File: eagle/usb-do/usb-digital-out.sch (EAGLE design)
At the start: 9 parts, among them IC2 PIC32MX795F512L, IC3 USB-UART-FT234XD, X2 MINI-USB-32005-201

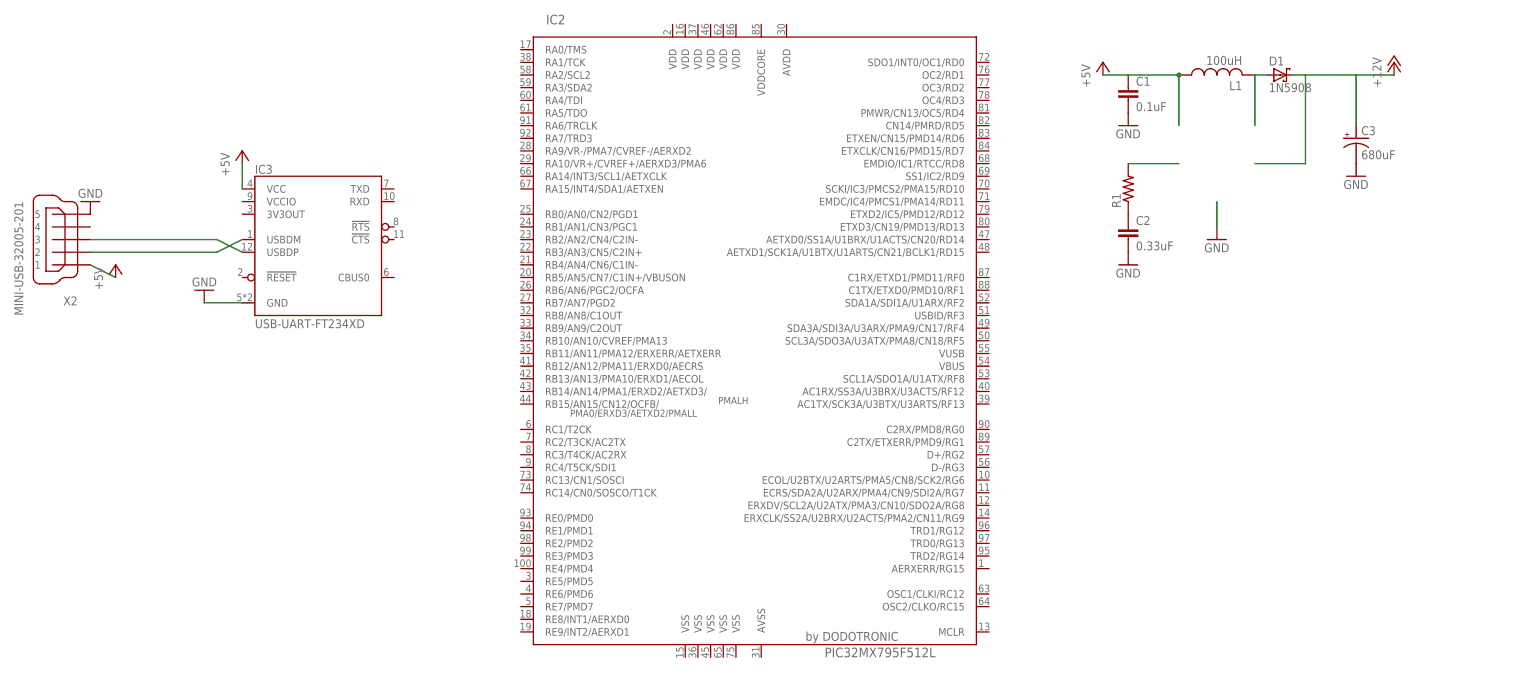
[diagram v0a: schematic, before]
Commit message: updated USB schematic with LM2577-12
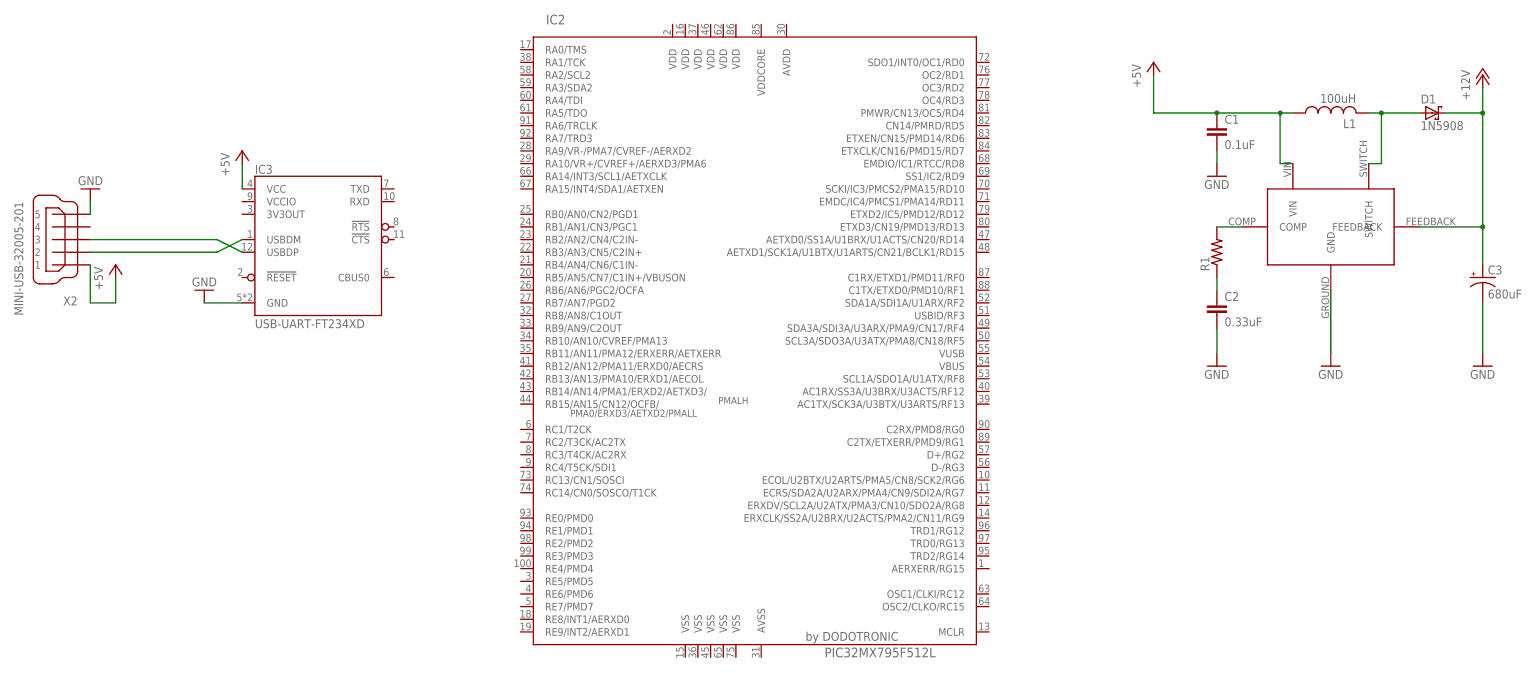
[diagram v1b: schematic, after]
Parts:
- added U$1: LM2577, nusolar_components:LM2577
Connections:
- net +12V: now also U$1.FEEDBACK
- net +5V: now also U$1.VIN
- net GND: now also U$1.GND
- net N$2: now also R1.2, U$1.COMP; no longer D1.A, L1.2
- net N$3: now also D1.A, L1.2, U$1.SWITCH; no longer R1.2
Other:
- moved on the sheet: C1, C2, C3, D1, L1, R1
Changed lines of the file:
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@@
 <part name="IC2" library="DodoMicroR3" deviceset="PIC32MX795F512" device="L"/>
 <part name="IC3" library="11-egna-ic" deviceset="USB-UART-FT234XD" device=""/>
+<part name="U$1" library="nusolar_components" deviceset="LM2577" device=""/>
 </parts>
 <sheets>
@@
 </plain>
 <instances>
-<instance part="P+1" gate="1" x="152.4" y="81.28"/>
-<instance part="C1" gate="G$1" x="157.48" y="76.2"/>
-<instance part="C2" gate="G$1" x="157.48" y="48.26"/>
-<instance part="GND1" gate="1" x="157.48" y="68.58"/>
-<instance part="GND2" gate="1" x="157.48" y="40.64"/>
-<instance part="GND3" gate="1" x="175.26" y="45.72"/>
-<instance part="GND4" gate="1" x="203.2" y="58.42"/>
-<instance part="R1" gate="G$1" x="157.48" y="55.88" rot="R90"/>
-<instance part="C3" gate="G$1" x="203.2" y="66.04"/>
-<instance part="L1" gate="G$1" x="175.26" y="78.74" rot="R90"/>
-<instance part="D1" gate="1" x="187.96" y="78.74"/>
-<instance part="P+2" gate="1" x="210.82" y="81.28"/>
+<instance part="P+1" gate="1" x="162.56" y="81.28"/>
+<instance part="C1" gate="G$1" x="175.26" y="68.58"/>
+<instance part="C2" gate="G$1" x="175.26" y="33.02"/>
+<instance part="GND1" gate="1" x="175.26" y="58.42"/>
+<instance part="GND2" gate="1" x="175.26" y="20.32"/>
+<instance part="GND3" gate="1" x="198.12" y="20.32"/>
+<instance part="GND4" gate="1" x="228.6" y="20.32"/>
+<instance part="R1" gate="G$1" x="175.26" y="43.18" rot="R90"/>
+<instance part="C3" gate="G$1" x="228.6" y="38.1"/>
+<instance part="L1" gate="G$1" x="198.12" y="71.12" rot="R90"/>
+<instance part="D1" gate="1" x="218.44" y="71.12"/>
+<instance part="P+2" gate="1" x="228.6" y="78.74"/>
 <instance part="X2" gate="G$1" x="-55.88" y="45.72" rot="R180"/>
 <instance part="P+3" gate="1" x="-45.72" y="40.64"/>
-<instance part="GND5" gate="1" x="-50.8" y="53.34" rot="R180"/>
+<instance part="GND5" gate="1" x="-50.8" y="55.88" rot="R180"/>
 <instance part="GND6" gate="1" x="-27.94" y="35.56" rot="R180"/>
 <instance part="P+4" gate="1" x="-20.32" y="63.5"/>
 <instance part="IC2" gate="G$1" x="86.36" y="22.86"/>
 <instance part="IC3" gate="G$1" x="-5.08" y="43.18"/>
+<instance part="U$1" gate="G$1" x="198.12" y="48.26"/>
 </instances>
 <busses>
@@
 <pinref part="GND1" gate="1" pin="GND"/>
 <pinref part="C1" gate="G$1" pin="2"/>
+<wire x1="175.26" y1="60.96" x2="175.26" y2="63.5" width="0.1524" layer="91"/>
 </segment>
 <segment>
 <pinref part="C2" gate="G$1" pin="2"/>
 <pinref part="GND2" gate="1" pin="GND"/>
+<wire x1="175.26" y1="22.86" x2="175.26" y2="27.94" width="0.1524" layer="91"/>
 </segment>
 <segment>
 <pinref part="GND4" gate="1" pin="GND"/>
 <pinref part="C3" gate="G$1" pin="-"/>
+<wire x1="228.6" y1="22.86" x2="228.6" y2="33.02" width="0.1524" layer="91"/>
 </segment>
 <segment>
 <pinref part="GND3" gate="1" pin="GND"/>
-<wire x1="175.26" y1="48.26" x2="175.26" y2="53.34" width="0.1524" layer="91"/>
+<wire x1="198.12" y1="22.86" x2="198.12" y2="35.56" width="0.1524" layer="91"/>
+<pinref part="U$1" gate="G$1" pin="GND"/>
 </segment>
 <segment>
 <pinref part="X2" gate="G$1" pin="5"/>
 <pinref part="GND5" gate="1" pin="GND"/>
+<wire x1="-50.8" y1="53.34" x2="-50.8" y2="50.8" width="0.1524" layer="91"/>
 </segment>
 <segment>
@@
 <net name="+5V" class="0">
 <segment>
+<pinref part="IC3" gate="G$1" pin="VCC"/>
+<pinref part="P+4" gate="1" pin="+5V"/>
+<wire x1="-20.32" y1="55.88" x2="-20.32" y2="60.96" width="0.1524" layer="91"/>
+</segment>
+<segment>
 <pinref part="P+1" gate="1" pin="+5V"/>
-<wire x1="152.4" y1="78.74" x2="157.48" y2="78.74" width="0.1524" layer="91"/>
+<wire x1="162.56" y1="78.74" x2="162.56" y2="71.12" width="0.1524" layer="91"/>
 <pinref part="C1" gate="G$1" pin="1"/>
+<wire x1="162.56" y1="71.12" x2="175.26" y2="71.12" width="0.1524" layer="91"/>
 <pinref part="L1" gate="G$1" pin="1"/>
-<junction x="167.64" y="78.74"/>
-<wire x1="167.64" y1="78.74" x2="157.48" y2="78.74" width="0.1524" layer="91"/>
-<wire x1="167.64" y1="78.74" x2="167.64" y2="68.58" width="0.1524" layer="91"/>
+<wire x1="175.26" y1="71.12" x2="187.96" y2="71.12" width="0.1524" layer="91"/>
+<junction x="175.26" y="71.12"/>
+<wire x1="187.96" y1="71.12" x2="190.5" y2="71.12" width="0.1524" layer="91"/>
+<wire x1="187.96" y1="71.12" x2="187.96" y2="60.96" width="0.1524" layer="91"/>
+<junction x="187.96" y="71.12"/>
+<pinref part="U$1" gate="G$1" pin="VIN"/>
+<wire x1="187.96" y1="60.96" x2="190.5" y2="60.96" width="0.1524" layer="91"/>
 </segment>
 <segment>
 <pinref part="X2" gate="G$1" pin="1"/>
+<wire x1="-50.8" y1="40.64" x2="-50.8" y2="33.02" width="0.1524" layer="91"/>
+<wire x1="-50.8" y1="33.02" x2="-45.72" y2="33.02" width="0.1524" layer="91"/>
 <pinref part="P+3" gate="1" pin="+5V"/>
-<wire x1="-50.8" y1="40.64" x2="-45.72" y2="38.1" width="0.1524" layer="91"/>
-</segment>
-<segment>
-<pinref part="IC3" gate="G$1" pin="VCC"/>
-<pinref part="P+4" gate="1" pin="+5V"/>
-<wire x1="-20.32" y1="55.88" x2="-20.32" y2="60.96" width="0.1524" layer="91"/>
+<wire x1="-45.72" y1="33.02" x2="-45.72" y2="38.1" width="0.1524" layer="91"/>
 </segment>
 </net>
@@
 <pinref part="C2" gate="G$1" pin="1"/>
 <pinref part="R1" gate="G$1" pin="1"/>
-</segment>
-</net>
-<net name="N$2" class="0">
-<segment>
-<pinref part="L1" gate="G$1" pin="2"/>
-<pinref part="D1" gate="1" pin="A"/>
-<wire x1="182.88" y1="78.74" x2="185.42" y2="78.74" width="0.1524" layer="91"/>
-<wire x1="182.88" y1="78.74" x2="182.88" y2="68.58" width="0.1524" layer="91"/>
-</segment>
-</net>
-<net name="+12V" class="0">
-<segment>
-<pinref part="P+2" gate="1" pin="+12V"/>
-<pinref part="D1" gate="1" pin="C"/>
-<wire x1="210.82" y1="78.74" x2="203.2" y2="78.74" width="0.1524" layer="91"/>
-<pinref part="C3" gate="G$1" pin="+"/>
-<wire x1="203.2" y1="78.74" x2="193.04" y2="78.74" width="0.1524" layer="91"/>
-<wire x1="193.04" y1="78.74" x2="190.5" y2="78.74" width="0.1524" layer="91"/>
-<wire x1="203.2" y1="68.58" x2="203.2" y2="78.74" width="0.1524" layer="91"/>
-<wire x1="193.04" y1="78.74" x2="193.04" y2="60.96" width="0.1524" layer="91"/>
-<wire x1="193.04" y1="60.96" x2="182.88" y2="60.96" width="0.1524" layer="91"/>
-</segment>
-</net>
-<net name="N$3" class="0">
-<segment>
-<pinref part="R1" gate="G$1" pin="2"/>
-<wire x1="157.48" y1="60.96" x2="167.64" y2="60.96" width="0.1524" layer="91"/>
+<wire x1="175.26" y1="35.56" x2="175.26" y2="38.1" width="0.1524" layer="91"/>
 </segment>
 </net>
@@
 </segment>
 </net>
+<net name="N$2" class="0">
+<segment>
+<pinref part="R1" gate="G$1" pin="2"/>
+<pinref part="U$1" gate="G$1" pin="COMP"/>
+<wire x1="175.26" y1="48.26" x2="180.34" y2="48.26" width="0.1524" layer="91"/>
+</segment>
+</net>
+<net name="N$3" class="0">
+<segment>
+<pinref part="L1" gate="G$1" pin="2"/>
+<pinref part="D1" gate="1" pin="A"/>
+<wire x1="205.74" y1="71.12" x2="208.28" y2="71.12" width="0.1524" layer="91"/>
+<pinref part="U$1" gate="G$1" pin="SWITCH"/>
+<wire x1="208.28" y1="71.12" x2="215.9" y2="71.12" width="0.1524" layer="91"/>
+<wire x1="205.74" y1="60.96" x2="208.28" y2="60.96" width="0.1524" layer="91"/>
+<wire x1="208.28" y1="60.96" x2="208.28" y2="71.12" width="0.1524" layer="91"/>
+<junction x="208.28" y="71.12"/>
+</segment>
+</net>
+<net name="+12V" class="0">
+<segment>
+<pinref part="D1" gate="1" pin="C"/>
+<wire x1="220.98" y1="71.12" x2="228.6" y2="71.12" width="0.1524" layer="91"/>
+<pinref part="P+2" gate="1" pin="+12V"/>
+<wire x1="228.6" y1="71.12" x2="228.6" y2="76.2" width="0.1524" layer="91"/>
+<pinref part="U$1" gate="G$1" pin="FEEDBACK"/>
+<pinref part="C3" gate="G$1" pin="+"/>
+<wire x1="215.9" y1="48.26" x2="228.6" y2="48.26" width="0.1524" layer="91"/>
+<wire x1="228.6" y1="48.26" x2="228.6" y2="40.64" width="0.1524" layer="91"/>
+<wire x1="228.6" y1="48.26" x2="228.6" y2="71.12" width="0.1524" layer="91"/>
+<junction x="228.6" y="48.26"/>
+<junction x="228.6" y="71.12"/>
+</segment>
+</net>
